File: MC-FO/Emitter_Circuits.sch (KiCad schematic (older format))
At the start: 10 parts, among them U27 74ACT08SCX, U28 IFE98

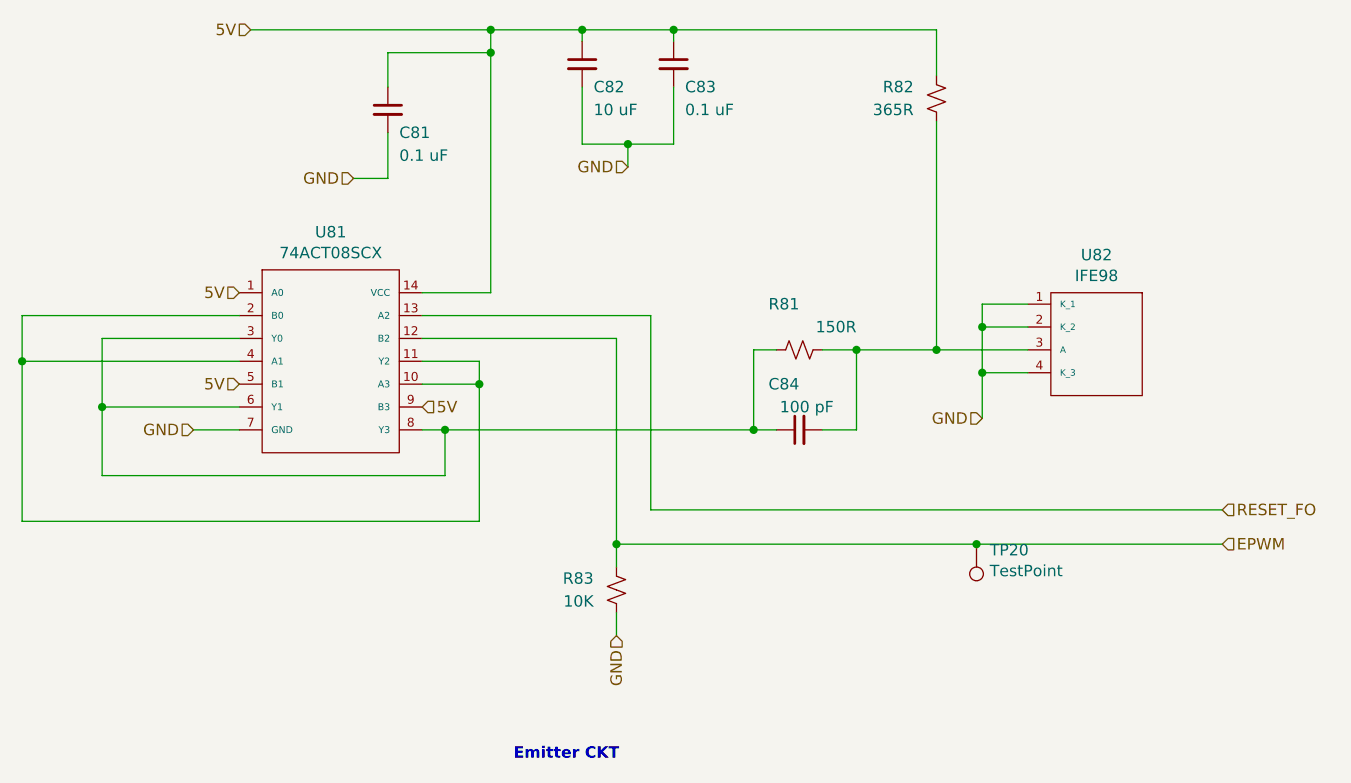
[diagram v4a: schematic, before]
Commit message: updating SAFE_STATE_FLAG and EMITTER_ENABLE
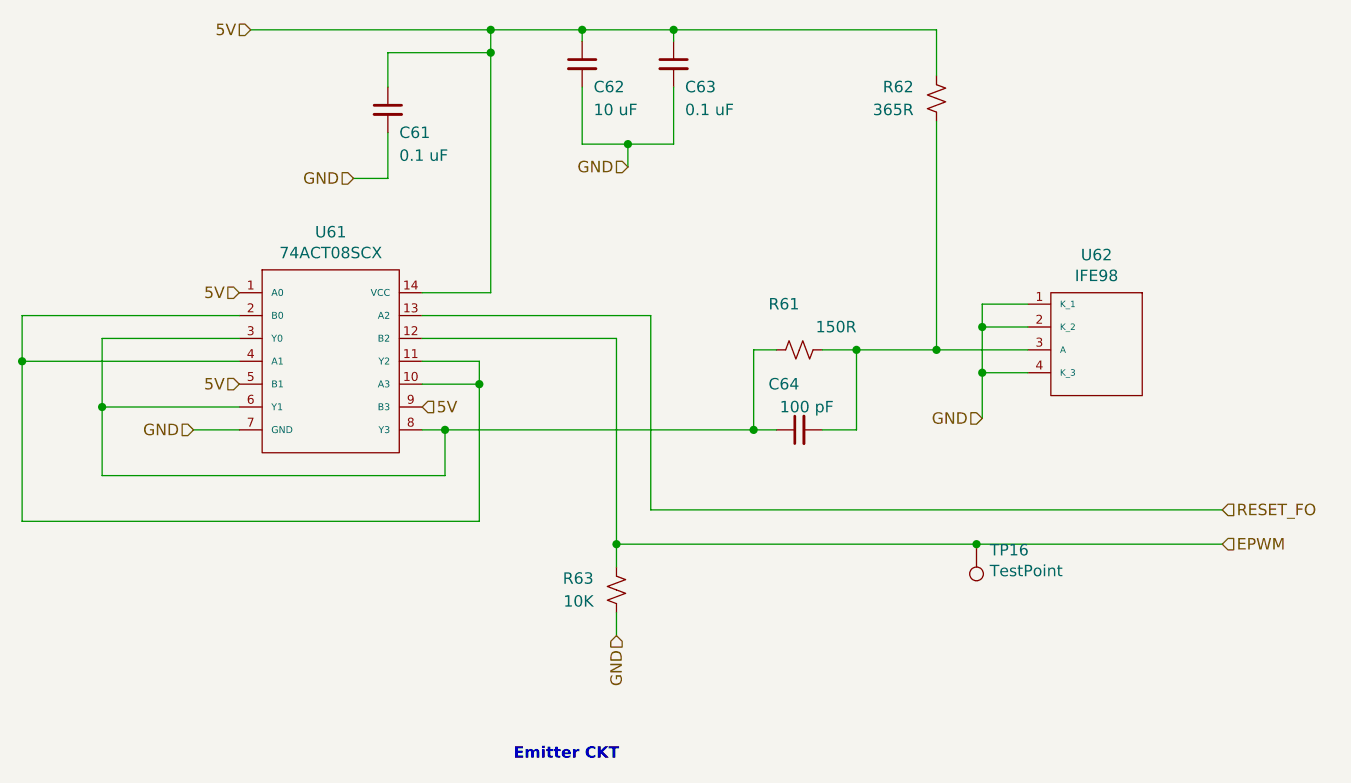
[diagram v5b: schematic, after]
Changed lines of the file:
@@
 $Descr A4 11693 8268
 encoding utf-8
-Sheet 4 11
+Sheet 6 11
 Title ""
 Date ""
@@
 AR Path="/6176CA81/617428A7" Ref="R101"  Part="1"
 AR Path="/6176CAE4/617428A7" Ref="R121"  Part="1"
-F 0 "R81" V 6900 4400 50  0000 L CNN
+F 0 "R61" V 6900 4400 50  0000 L CNN
 F 1 "150R" V 6800 4150 50  0000 L CNN
 F 2 "Resistor_SMD:R_0603_1608Metric" H 6700 4400 50  0001 C CNN
@@
 AR Path="/6176CA81/61748E58" Ref="C104"  Part="1"
 AR Path="/6176CAE4/61748E58" Ref="C124"  Part="1"
-F 0 "C84" V 6900 4750 50  0000 L CNN
+F 0 "C64" V 6900 4750 50  0000 L CNN
 F 1 "100 pF" V 6800 4600 50  0000 L CNN
 F 2 "Capacitor_SMD:C_0603_1608Metric" H 6700 4750 50  0001 C CNN
@@
 AR Path="/6176CA81/6178E7F7" Ref="R102"  Part="1"
 AR Path="/6176CAE4/6178E7F7" Ref="R122"  Part="1"
-F 0 "R82" H 7400 3250 50  0000 L CNN
+F 0 "R62" H 7400 3250 50  0000 L CNN
 F 1 "365R" H 7400 3350 50  0000 L CNN
 F 2 "Resistor_SMD:R_0603_1608Metric" H 7300 3300 50  0001 C CNN
@@
 AR Path="/6176CA81/6171F0C9" Ref="C101"  Part="1"
 AR Path="/6176CAE4/6171F0C9" Ref="C121"  Part="1"
-F 0 "C81" H 4950 3250 50  0000 L CNN
+F 0 "C61" H 4950 3250 50  0000 L CNN
 F 1 "0.1 uF" H 4950 3150 50  0000 L CNN
 F 2 "Capacitor_SMD:C_0603_1608Metric" H 4900 3350 50  0001 C CNN
@@
 AR Path="/6176CA81/61733718" Ref="C103"  Part="1"
 AR Path="/6176CAE4/61733718" Ref="C123"  Part="1"
-F 0 "C83" H 6200 3050 50  0000 L CNN
+F 0 "C63" H 6200 3050 50  0000 L CNN
 F 1 "0.1 uF" H 6200 2950 50  0000 L CNN
 F 2 "Capacitor_SMD:C_0603_1608Metric" H 6150 3150 50  0001 C CNN
@@
 AR Path="/6176CA81/61730A88" Ref="C102"  Part="1"
 AR Path="/6176CAE4/61730A88" Ref="C122"  Part="1"
-F 0 "C82" H 5800 3050 50  0000 L CNN
+F 0 "C62" H 5800 3050 50  0000 L CNN
 F 1 "10 uF" H 5800 2950 50  0000 L CNN
 F 2 "Capacitor_SMD:C_0603_1608Metric" H 5750 3150 50  0001 C CNN
@@
 AR Path="/6176CA81/61804FDE" Ref="U101"  Part="1"
 AR Path="/6176CAE4/61804FDE" Ref="U121"  Part="1"
-F 0 "U81" H 4650 4115 50  0000 C CNN
+F 0 "U61" H 4650 4115 50  0000 C CNN
 F 1 "74ACT08SCX" H 4650 4024 50  0000 C CNN
 F 2 "Package_SO:SOIC-14_3.9x8.7mm_P1.27mm" H 4650 4000 50  0001 C CNN
@@
 AR Path="/6176CAE4/61778B54" Ref="U122"  Part="1"
 AR Path="/617509F7/61778B54" Ref="U42"  Part="1"
-F 0 "U82" H 8000 4215 50  0000 C CNN
+F 0 "U62" H 8000 4215 50  0000 C CNN
 F 1 "IFE98" H 8000 4124 50  0000 C CNN
 F 2 "Footprints_MC-FO:IFE98" H 8000 4100 50  0001 C CNN
@@
 AR Path="/6176CA81/617DC24B" Ref="R103"  Part="1"
 AR Path="/6176CAE4/617DC24B" Ref="R123"  Part="1"
-F 0 "R83" H 6000 5400 50  0000 L CNN
+F 0 "R63" H 6000 5400 50  0000 L CNN
 F 1 "10K" H 6000 5500 50  0000 L CNN
 F 2 "Resistor_SMD:R_0603_1608Metric" H 5900 5450 50  0001 C CNN
@@
 AR Path="/61750A2A/623D825D" Ref="TP16"  Part="1"
 AR Path="/6176CA10/623D825D" Ref="TP20"  Part="1"
-F 0 "TP20" H 7417 5276 50  0000 R CNN
+F 0 "TP16" H 7417 5276 50  0000 R CNN
 F 1 "TestPoint" H 7417 5367 50  0000 R CNN
 F 2 "TestPoint:TestPoint_Pad_D2.0mm" H 7675 5250 50  0001 C CNN

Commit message: schematic changes--> layout rev
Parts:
- U21: renamed from U27; symbol Existing_IC_Models:74ACT08SCX -> MC-FO:74ACT08SCX
- renumbered C33 to C21, C34 to C22, C35 to C23, C36 to C24, R29 to R21, R27 to R22, R28 to R23, TP14 to TP21, U28 to U22
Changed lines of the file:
@@
 $Descr A4 11693 8268
 encoding utf-8
-Sheet 6 11
+Sheet 3 11
 Title ""
 Date ""
@@
 Emitter CKT
 $Comp
-L Device:R_Small_US R27
+L Device:R_Small_US R22
 U 1 1 617428A7
 P 6700 4400
-AR Path="/61717EAF/617428A7" Ref="R27"  Part="1"
+AR Path="/61717EAF/617428A7" Ref="R22"  Part="1"
 AR Path="/617509F7/617428A7" Ref="R41"  Part="1"
 AR Path="/61750A2A/617428A7" Ref="R61"  Part="1"
@@
 AR Path="/6176CA81/617428A7" Ref="R101"  Part="1"
 AR Path="/6176CAE4/617428A7" Ref="R121"  Part="1"
-F 0 "R61" V 6900 4400 50  0000 L CNN
+F 0 "R121" V 6900 4400 50  0000 L CNN
 F 1 "150R" V 6800 4150 50  0000 L CNN
 F 2 "Resistor_SMD:R_0603_1608Metric" H 6700 4400 50  0001 C CNN
@@
 $EndComp
 $Comp
-L Device:C_Small C36
+L Device:C_Small C24
 U 1 1 61748E58
 P 6700 4750
-AR Path="/61717EAF/61748E58" Ref="C36"  Part="1"
+AR Path="/61717EAF/61748E58" Ref="C24"  Part="1"
 AR Path="/617509F7/61748E58" Ref="C44"  Part="1"
 AR Path="/61750A2A/61748E58" Ref="C64"  Part="1"
@@
 AR Path="/6176CA81/61748E58" Ref="C104"  Part="1"
 AR Path="/6176CAE4/61748E58" Ref="C124"  Part="1"
-F 0 "C64" V 6900 4750 50  0000 L CNN
+F 0 "C124" V 6900 4750 50  0000 L CNN
 F 1 "100 pF" V 6800 4600 50  0000 L CNN
 F 2 "Capacitor_SMD:C_0603_1608Metric" H 6700 4750 50  0001 C CNN
@@
 	6950 4400 6800 4400
 $Comp
-L Device:R_Small_US R28
+L Device:R_Small_US R23
 U 1 1 6178E7F7
 P 7300 3300
-AR Path="/61717EAF/6178E7F7" Ref="R28"  Part="1"
+AR Path="/61717EAF/6178E7F7" Ref="R23"  Part="1"
 AR Path="/617509F7/6178E7F7" Ref="R42"  Part="1"
 AR Path="/61750A2A/6178E7F7" Ref="R62"  Part="1"
@@
 AR Path="/6176CA81/6178E7F7" Ref="R102"  Part="1"
 AR Path="/6176CAE4/6178E7F7" Ref="R122"  Part="1"
-F 0 "R62" H 7400 3250 50  0000 L CNN
+F 0 "R122" H 7400 3250 50  0000 L CNN
 F 1 "365R" H 7400 3350 50  0000 L CNN
 F 2 "Resistor_SMD:R_0603_1608Metric" H 7300 3300 50  0001 C CNN
@@
 	4900 3100 4900 3250
 $Comp
-L Device:C_Small C33
+L Device:C_Small C21
 U 1 1 6171F0C9
 P 4900 3350
-AR Path="/61717EAF/6171F0C9" Ref="C33"  Part="1"
+AR Path="/61717EAF/6171F0C9" Ref="C21"  Part="1"
 AR Path="/617509F7/6171F0C9" Ref="C41"  Part="1"
 AR Path="/61750A2A/6171F0C9" Ref="C61"  Part="1"
@@
 AR Path="/6176CA81/6171F0C9" Ref="C101"  Part="1"
 AR Path="/6176CAE4/6171F0C9" Ref="C121"  Part="1"
-F 0 "C61" H 4950 3250 50  0000 L CNN
+F 0 "C121" H 4950 3250 50  0000 L CNN
 F 1 "0.1 uF" H 4950 3150 50  0000 L CNN
 F 2 "Capacitor_SMD:C_0603_1608Metric" H 4900 3350 50  0001 C CNN
@@
 	5750 3500 5750 3250
 $Comp
-L Device:C_Small C35
+L Device:C_Small C23
 U 1 1 61733718
 P 6150 3150
-AR Path="/61717EAF/61733718" Ref="C35"  Part="1"
+AR Path="/61717EAF/61733718" Ref="C23"  Part="1"
 AR Path="/617509F7/61733718" Ref="C43"  Part="1"
 AR Path="/61750A2A/61733718" Ref="C63"  Part="1"
@@
 AR Path="/6176CA81/61733718" Ref="C103"  Part="1"
 AR Path="/6176CAE4/61733718" Ref="C123"  Part="1"
-F 0 "C63" H 6200 3050 50  0000 L CNN
+F 0 "C123" H 6200 3050 50  0000 L CNN
 F 1 "0.1 uF" H 6200 2950 50  0000 L CNN
 F 2 "Capacitor_SMD:C_0603_1608Metric" H 6150 3150 50  0001 C CNN
@@
 	5750 3000 5750 3050
 $Comp
-L Device:C_Small C34
+L Device:C_Small C22
 U 1 1 61730A88
 P 5750 3150
-AR Path="/61717EAF/61730A88" Ref="C34"  Part="1"
+AR Path="/61717EAF/61730A88" Ref="C22"  Part="1"
 AR Path="/617509F7/61730A88" Ref="C42"  Part="1"
 AR Path="/61750A2A/61730A88" Ref="C62"  Part="1"
@@
 AR Path="/6176CA81/61730A88" Ref="C102"  Part="1"
 AR Path="/6176CAE4/61730A88" Ref="C122"  Part="1"
-F 0 "C62" H 5800 3050 50  0000 L CNN
+F 0 "C122" H 5800 3050 50  0000 L CNN
 F 1 "10 uF" H 5800 2950 50  0000 L CNN
 F 2 "Capacitor_SMD:C_0603_1608Metric" H 5750 3150 50  0001 C CNN
@@
 	4900 3100 5350 3100
 Connection ~ 5350 3100
-Wire Wire Line
-	4050 4750 4250 4750
-$Comp
-L Existing_IC_Models:74ACT08SCX U27
+$Comp
+L MC-FO:74ACT08SCX U21
 U 1 1 61804FDE
 P 4650 4000
-AR Path="/61717EAF/61804FDE" Ref="U27"  Part="1"
+AR Path="/61717EAF/61804FDE" Ref="U21"  Part="1"
 AR Path="/617509F7/61804FDE" Ref="U41"  Part="1"
 AR Path="/61750A2A/61804FDE" Ref="U61"  Part="1"
@@
 AR Path="/6176CA81/61804FDE" Ref="U101"  Part="1"
 AR Path="/6176CAE4/61804FDE" Ref="U121"  Part="1"
-F 0 "U61" H 4650 4115 50  0000 C CNN
+F 0 "U121" H 4650 4115 50  0000 C CNN
 F 1 "74ACT08SCX" H 4650 4024 50  0000 C CNN
 F 2 "Package_SO:SOIC-14_3.9x8.7mm_P1.27mm" H 4650 4000 50  0001 C CNN
@@
 	5050 4350 5900 4350
 $Comp
-L Existing_IC_Models:IFE98 U28
+L Existing_IC_Models:IFE98 U22
 U 1 1 61778B54
 P 8000 4100
-AR Path="/61717EAF/61778B54" Ref="U28"  Part="1"
+AR Path="/61717EAF/61778B54" Ref="U22"  Part="1"
 AR Path="/61750A2A/61778B54" Ref="U62"  Part="1"
 AR Path="/6176CA10/61778B54" Ref="U82"  Part="1"
@@
 AR Path="/6176CAE4/61778B54" Ref="U122"  Part="1"
 AR Path="/617509F7/61778B54" Ref="U42"  Part="1"
-F 0 "U62" H 8000 4215 50  0000 C CNN
+F 0 "U122" H 8000 4215 50  0000 C CNN
 F 1 "IFE98" H 8000 4124 50  0000 C CNN
 F 2 "Footprints_MC-FO:IFE98" H 8000 4100 50  0001 C CNN
@@
 Connection ~ 6500 4750
 Wire Wire Line
-	5050 4450 5300 4450
-Wire Wire Line
-	5300 4450 5300 4550
-Wire Wire Line
 	5300 5150 3300 5150
 Wire Wire Line
@@
 Wire Wire Line
 	3650 4650 3650 4950
-Wire Wire Line
-	3300 4250 4250 4250
 Text HLabel 4250 4150 0    50   Input ~ 0
 5V
@@
 	3300 4450 3300 4250
 Wire Wire Line
-	5050 4550 5300 4550
-Connection ~ 5300 4550
-Wire Wire Line
-	5300 4550 5300 5150
-Wire Wire Line
 	4250 4350 3650 4350
 Wire Wire Line
@@
 	6050 4250 5050 4250
 $Comp
-L Device:R_Small_US R29
+L Device:R_Small_US R21
 U 1 1 617DC24B
 P 5900 5450
-AR Path="/61717EAF/617DC24B" Ref="R29"  Part="1"
+AR Path="/61717EAF/617DC24B" Ref="R21"  Part="1"
 AR Path="/617509F7/617DC24B" Ref="R43"  Part="1"
 AR Path="/61750A2A/617DC24B" Ref="R63"  Part="1"
@@
 AR Path="/6176CA81/617DC24B" Ref="R103"  Part="1"
 AR Path="/6176CAE4/617DC24B" Ref="R123"  Part="1"
-F 0 "R63" H 6000 5400 50  0000 L CNN
+F 0 "R123" H 6000 5400 50  0000 L CNN
 F 1 "10K" H 6000 5500 50  0000 L CNN
 F 2 "Resistor_SMD:R_0603_1608Metric" H 5900 5450 50  0001 C CNN
@@
 5V
 $Comp
-L Connector:TestPoint TP14
+L Connector:TestPoint TP21
 U 1 1 623D825D
 P 7475 5250
-AR Path="/61717EAF/623D825D" Ref="TP14"  Part="1"
-AR Path="/6176CA81/623D825D" Ref="TP12"  Part="1"
-AR Path="/6176CAE4/623D825D" Ref="TP13"  Part="1"
-AR Path="/617509F7/623D825D" Ref="TP15"  Part="1"
-AR Path="/61750A2A/623D825D" Ref="TP16"  Part="1"
-AR Path="/6176CA10/623D825D" Ref="TP20"  Part="1"
-F 0 "TP16" H 7417 5276 50  0000 R CNN
+AR Path="/61717EAF/623D825D" Ref="TP21"  Part="1"
+AR Path="/6176CA81/623D825D" Ref="TP101"  Part="1"
+AR Path="/6176CAE4/623D825D" Ref="TP121"  Part="1"
+AR Path="/617509F7/623D825D" Ref="TP41"  Part="1"
+AR Path="/61750A2A/623D825D" Ref="TP61"  Part="1"
+AR Path="/6176CA10/623D825D" Ref="TP81"  Part="1"
+F 0 "TP121" H 7275 5500 50  0000 R CNN
 F 1 "TestPoint" H 7417 5367 50  0000 R CNN
 F 2 "TestPoint:TestPoint_Pad_D2.0mm" H 7675 5250 50  0001 C CNN
@@
 Wire Wire Line
 	7475 5250 8550 5250
+Wire Wire Line
+	4250 4750 4050 4750
+Wire Wire Line
+	3300 4250 4250 4250
+Wire Wire Line
+	5300 4450 5050 4450
+Wire Wire Line
+	5300 4450 5300 4550
+Wire Wire Line
+	5300 4550 5050 4550
+Connection ~ 5300 4550
+Wire Wire Line
+	5300 4550 5300 5150
 $EndSCHEMATC

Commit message: Add files via upload
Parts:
- U21: symbol MC-FO:74ACT08SCX -> Existing_IC_Models:74ACT08SCX
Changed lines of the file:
@@
 $Descr A4 11693 8268
 encoding utf-8
-Sheet 3 11
+Sheet 4 11
 Title ""
 Date ""
@@
 AR Path="/6176CA81/617428A7" Ref="R101"  Part="1"
 AR Path="/6176CAE4/617428A7" Ref="R121"  Part="1"
-F 0 "R121" V 6900 4400 50  0000 L CNN
+F 0 "R22" V 6900 4400 50  0000 L CNN
 F 1 "150R" V 6800 4150 50  0000 L CNN
 F 2 "Resistor_SMD:R_0603_1608Metric" H 6700 4400 50  0001 C CNN
@@
 AR Path="/6176CA81/61748E58" Ref="C104"  Part="1"
 AR Path="/6176CAE4/61748E58" Ref="C124"  Part="1"
-F 0 "C124" V 6900 4750 50  0000 L CNN
+F 0 "C24" V 6900 4750 50  0000 L CNN
 F 1 "100 pF" V 6800 4600 50  0000 L CNN
 F 2 "Capacitor_SMD:C_0603_1608Metric" H 6700 4750 50  0001 C CNN
@@
 AR Path="/6176CA81/6178E7F7" Ref="R102"  Part="1"
 AR Path="/6176CAE4/6178E7F7" Ref="R122"  Part="1"
-F 0 "R122" H 7400 3250 50  0000 L CNN
+F 0 "R23" H 7400 3250 50  0000 L CNN
 F 1 "365R" H 7400 3350 50  0000 L CNN
 F 2 "Resistor_SMD:R_0603_1608Metric" H 7300 3300 50  0001 C CNN
@@
 AR Path="/6176CA81/6171F0C9" Ref="C101"  Part="1"
 AR Path="/6176CAE4/6171F0C9" Ref="C121"  Part="1"
-F 0 "C121" H 4950 3250 50  0000 L CNN
+F 0 "C21" H 4950 3250 50  0000 L CNN
 F 1 "0.1 uF" H 4950 3150 50  0000 L CNN
 F 2 "Capacitor_SMD:C_0603_1608Metric" H 4900 3350 50  0001 C CNN
@@
 AR Path="/6176CA81/61733718" Ref="C103"  Part="1"
 AR Path="/6176CAE4/61733718" Ref="C123"  Part="1"
-F 0 "C123" H 6200 3050 50  0000 L CNN
+F 0 "C23" H 6200 3050 50  0000 L CNN
 F 1 "0.1 uF" H 6200 2950 50  0000 L CNN
 F 2 "Capacitor_SMD:C_0603_1608Metric" H 6150 3150 50  0001 C CNN
@@
 AR Path="/6176CA81/61730A88" Ref="C102"  Part="1"
 AR Path="/6176CAE4/61730A88" Ref="C122"  Part="1"
-F 0 "C122" H 5800 3050 50  0000 L CNN
+F 0 "C22" H 5800 3050 50  0000 L CNN
 F 1 "10 uF" H 5800 2950 50  0000 L CNN
 F 2 "Capacitor_SMD:C_0603_1608Metric" H 5750 3150 50  0001 C CNN
@@
 Connection ~ 5350 3100
 $Comp
-L MC-FO:74ACT08SCX U21
+L Existing_IC_Models:74ACT08SCX U21
 U 1 1 61804FDE
 P 4650 4000
@@
 AR Path="/6176CA81/61804FDE" Ref="U101"  Part="1"
 AR Path="/6176CAE4/61804FDE" Ref="U121"  Part="1"
-F 0 "U121" H 4650 4115 50  0000 C CNN
+AR Path="/61804FDE" Ref="U121"  Part="1"
+F 0 "U21" H 4650 4115 50  0000 C CNN
 F 1 "74ACT08SCX" H 4650 4024 50  0000 C CNN
 F 2 "Package_SO:SOIC-14_3.9x8.7mm_P1.27mm" H 4650 4000 50  0001 C CNN
@@
 AR Path="/6176CAE4/61778B54" Ref="U122"  Part="1"
 AR Path="/617509F7/61778B54" Ref="U42"  Part="1"
-F 0 "U122" H 8000 4215 50  0000 C CNN
+F 0 "U22" H 8000 4215 50  0000 C CNN
 F 1 "IFE98" H 8000 4124 50  0000 C CNN
 F 2 "Footprints_MC-FO:IFE98" H 8000 4100 50  0001 C CNN
@@
 AR Path="/6176CA81/617DC24B" Ref="R103"  Part="1"
 AR Path="/6176CAE4/617DC24B" Ref="R123"  Part="1"
-F 0 "R123" H 6000 5400 50  0000 L CNN
+F 0 "R21" H 6000 5400 50  0000 L CNN
 F 1 "10K" H 6000 5500 50  0000 L CNN
 F 2 "Resistor_SMD:R_0603_1608Metric" H 5900 5450 50  0001 C CNN
@@
 AR Path="/61750A2A/623D825D" Ref="TP61"  Part="1"
 AR Path="/6176CA10/623D825D" Ref="TP81"  Part="1"
-F 0 "TP121" H 7275 5500 50  0000 R CNN
+F 0 "TP21" H 7275 5500 50  0000 R CNN
 F 1 "TestPoint" H 7417 5367 50  0000 R CNN
 F 2 "TestPoint:TestPoint_Pad_D2.0mm" H 7675 5250 50  0001 C CNN
